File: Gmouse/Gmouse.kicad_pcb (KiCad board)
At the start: 2 copper layers, 121 x 100 mm, 1 part, among them U1 Teensy4.0

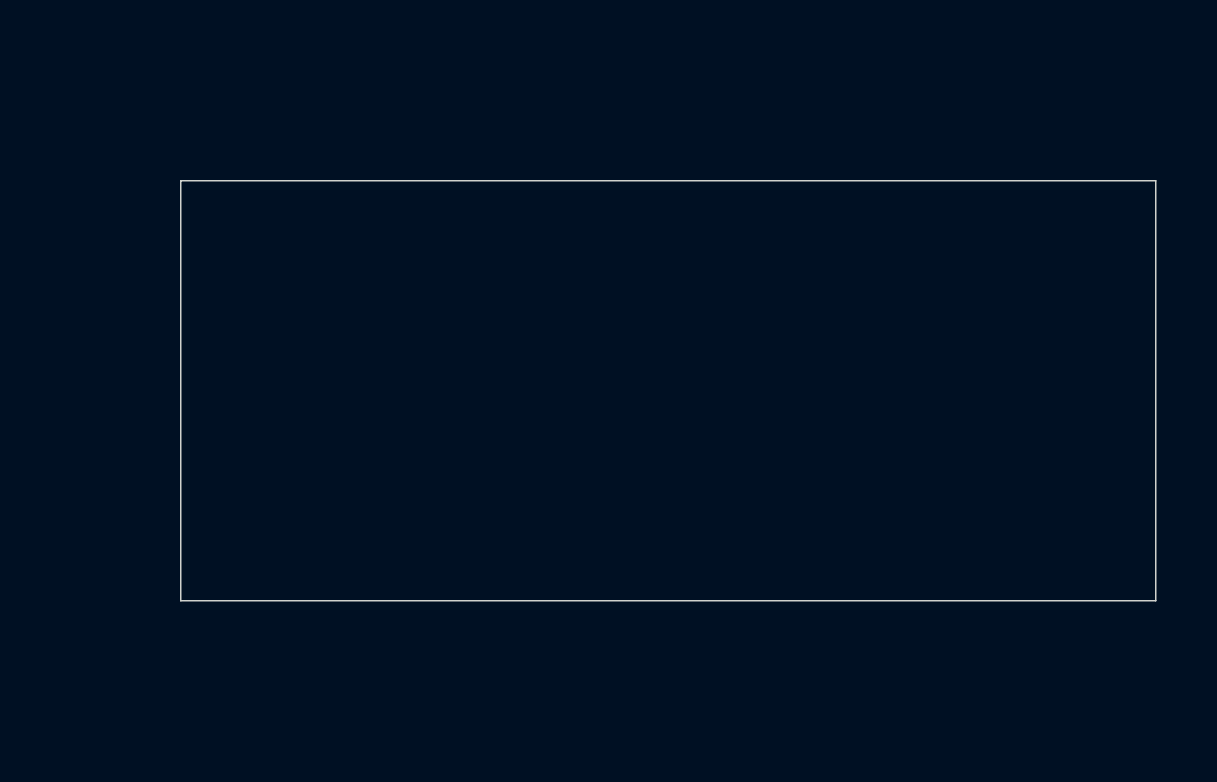
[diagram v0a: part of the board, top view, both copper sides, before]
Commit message: Adds basic motor circuitry and connectors, includes LED Display
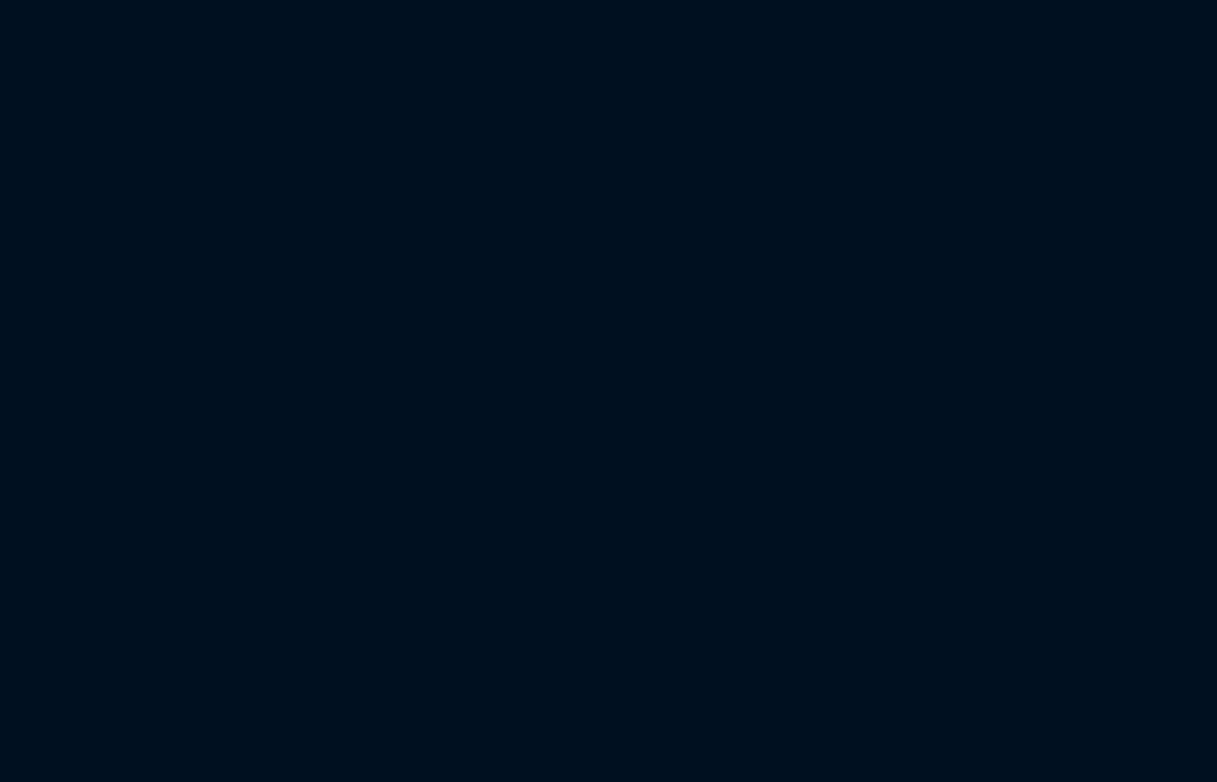
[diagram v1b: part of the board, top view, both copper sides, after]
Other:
- board size 121 x 100 mm -> 80 x 100 mm
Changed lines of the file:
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@@
 (kicad_pcb
-	(version 20240108)
+	(version 20241229)
 	(generator "pcbnew")
-	(generator_version "8.0")
+	(generator_version "9.0")
 	(general
 		(thickness 1.6)
@@
 	(layers
 		(0 "F.Cu" signal)
-		(31 "B.Cu" signal)
-		(32 "B.Adhes" user "B.Adhesive")
-		(33 "F.Adhes" user "F.Adhesive")
-		(34 "B.Paste" user)
-		(35 "F.Paste" user)
-		(36 "B.SilkS" user "B.Silkscreen")
-		(37 "F.SilkS" user "F.Silkscreen")
-		(38 "B.Mask" user)
-		(39 "F.Mask" user)
-		(40 "Dwgs.User" user "User.Drawings")
-		(41 "Cmts.User" user "User.Comments")
-		(42 "Eco1.User" user "User.Eco1")
-		(43 "Eco2.User" user "User.Eco2")
-		(44 "Edge.Cuts" user)
-		(45 "Margin" user)
-		(46 "B.CrtYd" user "B.Courtyard")
-		(47 "F.CrtYd" user "F.Courtyard")
-		(48 "B.Fab" user)
-		(49 "F.Fab" user)
-		(50 "User.1" user)
-		(51 "User.2" user)
-		(52 "User.3" user)
-		(53 "User.4" user)
-		(54 "User.5" user)
-		(55 "User.6" user)
-		(56 "User.7" user)
-		(57 "User.8" user)
-		(58 "User.9" user)
+		(2 "B.Cu" signal)
+		(9 "F.Adhes" user "F.Adhesive")
+		(11 "B.Adhes" user "B.Adhesive")
+		(13 "F.Paste" user)
+		(15 "B.Paste" user)
+		(5 "F.SilkS" user "F.Silkscreen")
+		(7 "B.SilkS" user "B.Silkscreen")
+		(1 "F.Mask" user)
+		(3 "B.Mask" user)
+		(17 "Dwgs.User" user "User.Drawings")
+		(19 "Cmts.User" user "User.Comments")
+		(21 "Eco1.User" user "User.Eco1")
+		(23 "Eco2.User" user "User.Eco2")
+		(25 "Edge.Cuts" user)
+		(27 "Margin" user)
+		(31 "F.CrtYd" user "F.Courtyard")
+		(29 "B.CrtYd" user "B.Courtyard")
+		(35 "F.Fab" user)
+		(33 "B.Fab" user)
+		(39 "User.1" user)
+		(41 "User.2" user)
+		(43 "User.3" user)
+		(45 "User.4" user)
+		(47 "User.5" user)
+		(49 "User.6" user)
+		(51 "User.7" user)
+		(53 "User.8" user)
+		(55 "User.9" user)
 	)
 	(setup
 		(pad_to_mask_clearance 0)
 		(allow_soldermask_bridges_in_footprints no)
+		(tenting front back)
 		(pcbplotparams
-			(layerselection 0x00010fc_ffffffff)
-			(plot_on_all_layers_selection 0x0000000_00000000)
+			(layerselection 0x00000000_00000000_55555555_5755f5ff)
+			(plot_on_all_layers_selection 0x00000000_00000000_00000000_00000000)
 			(disableapertmacros no)
 			(usegerberextensions no)
@@
 			(svgprecision 4)
 			(plotframeref no)
-			(viasonmask no)
 			(mode 1)
 			(useauxorigin no)
@@
 			(pdf_front_fp_property_popups yes)
 			(pdf_back_fp_property_popups yes)
+			(pdf_metadata yes)
+			(pdf_single_document no)
 			(dxfpolygonmode yes)
 			(dxfimperialunits yes)
@@
 			(psnegative no)
 			(psa4output no)
-			(plotreference yes)
-			(plotvalue yes)
-			(plotfptext yes)
+			(plot_black_and_white yes)
 			(plotinvisibletext no)
 			(sketchpadsonfab no)
+			(plotpadnumbers no)
+			(hidednponfab no)
+			(sketchdnponfab yes)
+			(crossoutdnponfab yes)
 			(subtractmaskfromsilk no)
 			(outputformat 1)
@@
 		(at 80 60 180)
 		(property "Reference" "U1"
-			(at 0 -10.16 360)
+			(at 0 -10.16 0)
 			(layer "F.SilkS")
 			(effects
@@
 		)
 		(property "Value" "Teensy4.0"
-			(at 0 10.16 360)
+			(at 0 10.16 0)
 			(layer "F.Fab")
 			(effects
@@
 			)
 		)
-		(property "Footprint" "Teensy:Teensy40_SMT"
-			(at 0 0 360)
+		(property "Datasheet" ""
+			(at 0 0 0)
 			(layer "F.Fab")
 			(hide yes)
@@
 			)
 		)
-		(property "Datasheet" ""
-			(at 0 0 360)
+		(property "Description" ""
+			(at 0 0 0)
 			(layer "F.Fab")
 			(hide yes)
@@
 			)
 		)
-		(property "Description" ""
-			(at 0 0 360)
-			(layer "F.Fab")
-			(hide yes)
-			(effects
-				(font
-					(size 1.27 1.27)
-					(thickness 0.15)
-				)
-			)
-		)
 		(sheetname "Root")
 		(sheetfile "Gmouse.kicad_sch")
@@
 				(type solid)
 			)
-			(fill solid)
+			(fill yes)
 			(layer "Eco1.User")
 		)
@@
 				(type solid)
 			)
-			(fill solid)
+			(fill yes)
 			(layer "Eco1.User")
 		)
@@
 				(type solid)
 			)
-			(fill solid)
+			(fill yes)
 			(layer "Eco1.User")
 		)
@@
 				(type solid)
 			)
-			(fill solid)
+			(fill yes)
 			(layer "Eco1.User")
 		)
@@
 				(type solid)
 			)
-			(fill solid)
+			(fill yes)
 			(layer "Eco1.User")
 		)
@@
 				(type solid)
 			)
-			(fill solid)
+			(fill yes)
 			(layer "Eco1.User")
 		)
@@
 				(type solid)
 			)
-			(fill solid)
+			(fill yes)
 			(layer "Eco1.User")
 		)
@@
 				(type solid)
 			)
-			(fill solid)
+			(fill yes)
 			(layer "Eco1.User")
 		)
@@
 				(type solid)
 			)
-			(fill solid)
+			(fill yes)
 			(layer "Eco1.User")
 		)
@@
 				(type solid)
 			)
-			(fill solid)
+			(fill yes)
 			(layer "Eco1.User")
 		)
@@
 				(type solid)
 			)
-			(fill solid)
+			(fill yes)
 			(layer "Eco1.User")
 		)
@@
 				(type solid)
 			)
-			(fill solid)
+			(fill yes)
 			(layer "Eco1.User")
 		)
@@
 				(type solid)
 			)
-			(fill solid)
+			(fill yes)
 			(layer "Eco1.User")
 		)
@@
 				(type solid)
 			)
-			(fill solid)
+			(fill yes)
 			(layer "Eco1.User")
 		)
@@
 				(type solid)
 			)
-			(fill solid)
+			(fill yes)
 			(layer "Eco1.User")
 		)
@@
 				(type solid)
 			)
-			(fill solid)
+			(fill yes)
 			(layer "Eco1.User")
 		)
@@
 				(type solid)
 			)
-			(fill solid)
+			(fill yes)
 			(layer "Eco1.User")
 		)
@@
 				(type solid)
 			)
-			(fill solid)
+			(fill yes)
 			(layer "Eco1.User")
 		)
@@
 				(type solid)
 			)
-			(fill solid)
+			(fill yes)
 			(layer "Eco1.User")
 		)
@@
 				(type solid)
 			)
-			(fill solid)
+			(fill yes)
 			(layer "Eco1.User")
 		)
@@
 			(pintype "bidirectional")
 		)
+		(embedded_fonts no)
 		(model "${KICAD_USER_DIR}/teensy.pretty/Teensy_4.0_Assembly.STEP"
 			(offset
@@
 			(type default)
 		)
-		(layer "Edge.Cuts")
-	)
-	(gr_rect
-		(start 128.5 62)
-		(end 161 76)
-		(stroke
-			(width 0.05)
-			(type default)
-		)
-		(fill none)
 		(layer "Edge.Cuts")
 	)
@@
 		(layer "Edge.Cuts")
 	)
+	(embedded_fonts no)
 )

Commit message: Pushing for desktop
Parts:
- moved U1 14.1 mm to (94.0, 58.0)
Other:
- outline, holes or cut-outs redrawn
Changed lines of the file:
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@@
 	(footprint "Teensy:Teensy40_SMT"
 		(layer "F.Cu")
-		(at 80 60 180)
+		(at 94 58 180)
 		(property "Reference" "U1"
 			(at 0 -10.16 0)
@@
 		(layer "Edge.Cuts")
 	)
-	(gr_arc
-		(start 40 70)
-		(mid 80 30)
-		(end 120 70)
+	(gr_line
+		(start 80 130)
+		(end 80 30)
+		(stroke
+			(width 0.05)
+			(type default)
+		)
+		(layer "Edge.Cuts")
+	)
+	(gr_curve
+		(pts
+			(xy 80 30) (xy 120 30) (xy 120 30) (xy 120 50)
+		)
 		(stroke
 			(width 0.05)
@@
 			(type default)
 		)
+		(locked yes)
+		(layer "Edge.Cuts")
+	)
+	(gr_curve
+		(pts
+			(xy 80 30) (xy 40 30) (xy 40 30) (xy 40 50)
+		)
+		(stroke
+			(width 0.05)
+			(type default)
+		)
 		(layer "Edge.Cuts")
 	)
@@
 	)
 	(gr_line
+		(start 40 50)
+		(end 40 70)
+		(stroke
+			(width 0.05)
+			(type default)
+		)
+		(layer "Edge.Cuts")
+	)
+	(gr_line
 		(start 106 70)
 		(end 120 70)
@@
 		(stroke
 			(width 0.05)
+			(type default)
+		)
+		(layer "Edge.Cuts")
+	)
+	(gr_line
+		(start 120 50)
+		(end 120 70)
+		(stroke
+			(width 0.05)

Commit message: Work Done Over Break
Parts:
- added BT1: 3.7V, Connector_JST:JST_PH_B2B-PH-K_1x02_P2.00mm_Vertical, F.Cu at (201.7, 83.1)
- added BT2: 3.7V, Connector_JST:JST_PH_B2B-PH-K_1x02_P2.00mm_Vertical, F.Cu at (201.7, 89.6)
- added C11: 4.7uF, Capacitor_SMD:C_1206_3216Metric_Pad1.33x1.80mm_HandSolder, F.Cu at (179.1, 82.0)
- added C12: 0.1uF, Capacitor_SMD:C_1206_3216Metric_Pad1.33x1.80mm_HandSolder, F.Cu at (179.1, 85.4)
- added C13: 4.7uF, Capacitor_SMD:C_1206_3216Metric_Pad1.33x1.80mm_HandSolder, F.Cu at (179.1, 88.7)
- added C14: 0.1uF, Capacitor_SMD:C_1206_3216Metric_Pad1.33x1.80mm_HandSolder, F.Cu at (179.1, 92.1)
- added C15: 4.7uF, Capacitor_SMD:C_1206_3216Metric_Pad1.33x1.80mm_HandSolder, F.Cu at (179.1, 95.4)
- added C16: 0.1uF, Capacitor_SMD:C_1206_3216Metric_Pad1.33x1.80mm_HandSolder, F.Cu at (179.1, 98.8)
- added C17: 4.7uF, Capacitor_SMD:C_1206_3216Metric_Pad1.33x1.80mm_HandSolder, F.Cu at (185.1, 82.0)
- added C18: 0.1uF, Capacitor_SMD:C_1206_3216Metric_Pad1.33x1.80mm_HandSolder, F.Cu at (185.1, 85.4)
- added C19: 4.7uF, Capacitor_SMD:C_1206_3216Metric_Pad1.33x1.80mm_HandSolder, F.Cu at (185.1, 88.7)
- added C2: 0.1 uF, Capacitor_SMD:C_1206_3216Metric_Pad1.33x1.80mm_HandSolder, F.Cu at (173.1, 82.0)
- added C20: 0.1uF, Capacitor_SMD:C_1206_3216Metric_Pad1.33x1.80mm_HandSolder, F.Cu at (185.1, 92.1)
- added C4: 0.1 uF, Capacitor_SMD:C_1206_3216Metric_Pad1.33x1.80mm_HandSolder, F.Cu at (173.1, 85.4)
- added C5: 4.7uF, Capacitor_SMD:C_1206_3216Metric_Pad1.33x1.80mm_HandSolder, F.Cu at (173.1, 88.7)
- added C6: 0.1uF, Capacitor_SMD:C_1206_3216Metric_Pad1.33x1.80mm_HandSolder, F.Cu at (173.1, 92.1)
- added C7: 0.1 uF, Capacitor_SMD:C_1206_3216Metric_Pad1.33x1.80mm_HandSolder, F.Cu at (173.1, 95.4)
- added C9: 0.1 uF, Capacitor_SMD:C_1206_3216Metric_Pad1.33x1.80mm_HandSolder, F.Cu at (173.1, 98.8)
- added D1: IR, LED_THT:LED_D5.0mm_Horizontal_O1.27mm_Z9.0mm, F.Cu at (142.6, 40.1)
- added D2: IR, LED_THT:LED_D5.0mm_Horizontal_O1.27mm_Z9.0mm, F.Cu at (150.1, 40.1)
- added D3: IR, LED_THT:LED_D5.0mm_Horizontal_O1.27mm_Z9.0mm, F.Cu at (157.6, 40.1)
- added D4: IR, LED_THT:LED_D5.0mm_Horizontal_O1.27mm_Z9.0mm, F.Cu at (165.1, 40.1)
- added D5: IR, LED_THT:LED_D5.0mm_Horizontal_O1.27mm_Z9.0mm, F.Cu at (142.6, 52.6)
- added D6: IR, LED_THT:LED_D5.0mm_Horizontal_O1.27mm_Z9.0mm, F.Cu at (150.1, 52.6)
- added J1: Motor_RF, Connector_JST:JST_SH_BM05B-SRSS-TB_1x05-1MP_P1.00mm_Vertical, F.Cu at (145.1, 78.8)
- added J2: Motor_RR, Connector_JST:JST_SH_BM05B-SRSS-TB_1x05-1MP_P1.00mm_Vertical, F.Cu at (145.1, 85.1)
- added J3: Motor_LF, Connector_JST:JST_SH_BM05B-SRSS-TB_1x05-1MP_P1.00mm_Vertical, F.Cu at (145.1, 91.3)
- added J4: Motor_LR, Connector_JST:JST_SH_BM05B-SRSS-TB_1x05-1MP_P1.00mm_Vertical, F.Cu at (145.1, 97.6)
- added J5: Conn_01x08_Pin, Connector_PinSocket_2.54mm:PinSocket_1x08_P2.54mm_Vertical, F.Cu at (85.2, 57.0)
- added LS1: SMT-0440-T-R, SMT_0440:XDCR_SMT-0440-T-R, F.Cu at (198.5, 68.4)
- added Q10: SFH300, LED_THT:LED_D5.0mm_Horizontal_O1.27mm_Z3.0mm_IRGrey, F.Cu at (157.6, 65.0)
- added Q12: SFH300, LED_THT:LED_D5.0mm_Horizontal_O1.27mm_Z3.0mm_IRGrey, F.Cu at (165.1, 65.0)
- added Q14: BC847, Package_TO_SOT_SMD:SOT-23, F.Cu at (202.5, 73.6)
- added Q2: SFH300, LED_THT:LED_D5.0mm_Horizontal_O1.27mm_Z3.0mm_IRGrey, F.Cu at (157.6, 52.6)
- added Q4: SFH300, LED_THT:LED_D5.0mm_Horizontal_O1.27mm_Z3.0mm_IRGrey, F.Cu at (165.1, 52.6)
- added Q6: SFH300, LED_THT:LED_D5.0mm_Horizontal_O1.27mm_Z3.0mm_IRGrey, F.Cu at (142.6, 65.0)
- added Q8: SFH300, LED_THT:LED_D5.0mm_Horizontal_O1.27mm_Z3.0mm_IRGrey, F.Cu at (150.1, 65.0)
- added R1: 47K, Resistor_SMD:R_1206_3216Metric_Pad1.30x1.75mm_HandSolder, F.Cu at (173.1, 59.0)
- added R10: 47K, Resistor_SMD:R_1206_3216Metric_Pad1.30x1.75mm_HandSolder, F.Cu at (179.0, 65.5)
- added R11: 51, Resistor_SMD:R_1206_3216Metric_Pad1.30x1.75mm_HandSolder, F.Cu at (179.0, 68.8)
- added R12: 1.8K, Resistor_SMD:R_1206_3216Metric_Pad1.30x1.75mm_HandSolder, F.Cu at (179.0, 72.1)
- added R13: 100, Resistor_SMD:R_1206_3216Metric_Pad1.30x1.75mm_HandSolder, F.Cu at (179.0, 75.4)
- added R14: 47K, Resistor_SMD:R_1206_3216Metric_Pad1.30x1.75mm_HandSolder, F.Cu at (179.0, 78.7)
- added R15: 51, Resistor_SMD:R_1206_3216Metric_Pad1.30x1.75mm_HandSolder, F.Cu at (185.0, 59.0)
- added R16: 1.8K, Resistor_SMD:R_1206_3216Metric_Pad1.30x1.75mm_HandSolder, F.Cu at (185.0, 62.3)
- added R17: 100, Resistor_SMD:R_1206_3216Metric_Pad1.30x1.75mm_HandSolder, F.Cu at (185.0, 65.5)
- added R18: 47K, Resistor_SMD:R_1206_3216Metric_Pad1.30x1.75mm_HandSolder, F.Cu at (185.0, 68.8)
- added R19: 51, Resistor_SMD:R_1206_3216Metric_Pad1.30x1.75mm_HandSolder, F.Cu at (185.0, 72.1)
- added R2: 100, Resistor_SMD:R_1206_3216Metric_Pad1.30x1.75mm_HandSolder, F.Cu at (173.1, 62.3)
- added R20: 1.8K, Resistor_SMD:R_1206_3216Metric_Pad1.30x1.75mm_HandSolder, F.Cu at (185.0, 75.4)
- added R21: 100, Resistor_SMD:R_1206_3216Metric_Pad1.30x1.75mm_HandSolder, F.Cu at (185.0, 78.7)
- added R22: 47K, Resistor_SMD:R_1206_3216Metric_Pad1.30x1.75mm_HandSolder, F.Cu at (190.9, 59.0)
- added R23: 51, Resistor_SMD:R_1206_3216Metric_Pad1.30x1.75mm_HandSolder, F.Cu at (190.9, 62.3)
- added R24: 1.8K, Resistor_SMD:R_1206_3216Metric_Pad1.30x1.75mm_HandSolder, F.Cu at (190.9, 65.5)
- added R25: 180, Resistor_SMD:R_1206_3216Metric_Pad1.30x1.75mm_HandSolder, F.Cu at (190.9, 68.8)
- added R3: 51, Resistor_SMD:R_1206_3216Metric_Pad1.30x1.75mm_HandSolder, F.Cu at (173.1, 65.5)
- added R4: 1.8K, Resistor_SMD:R_1206_3216Metric_Pad1.30x1.75mm_HandSolder, F.Cu at (173.1, 68.8)
- added R5: 100, Resistor_SMD:R_1206_3216Metric_Pad1.30x1.75mm_HandSolder, F.Cu at (173.1, 72.1)
- added R6: 47K, Resistor_SMD:R_1206_3216Metric_Pad1.30x1.75mm_HandSolder, F.Cu at (173.1, 75.4)
- added R7: 51, Resistor_SMD:R_1206_3216Metric_Pad1.30x1.75mm_HandSolder, F.Cu at (173.1, 78.7)
- added R8: 1.8K, Resistor_SMD:R_1206_3216Metric_Pad1.30x1.75mm_HandSolder, F.Cu at (179.0, 59.0)
- added R9: 100, Resistor_SMD:R_1206_3216Metric_Pad1.30x1.75mm_HandSolder, F.Cu at (179.0, 62.3)
- added REF**: JST_PH_B2B-PH-K_1x02_P2.00mm_Vertical, Connector_JST:JST_PH_B2B-PH-K_1x02_P2.00mm_Vertical, F.Cu at (66.0, 68.0)
- added REF**: JST_SH_BM06B-SRSS-TB_1x06-1MP_P1.00mm_Vertical, Connector_JST:JST_SH_BM06B-SRSS-TB_1x06-1MP_P1.00mm_Vertical, F.Cu at (91.0, 134.0)
- added REF**: JST_SH_BM06B-SRSS-TB_1x06-1MP_P1.00mm_Vertical, Connector_JST:JST_SH_BM06B-SRSS-TB_1x06-1MP_P1.00mm_Vertical, F.Cu at (73.0, 134.0)
- added REF**: DIP12_HCMS-290X-A_BRA, HCMS_2903:DIP12_HCMS-290X-A_BRA, F.Cu at (98.0, 137.0)
- added REF**: JST_SH_BM06B-SRSS-TB_1x06-1MP_P1.00mm_Vertical, Connector_JST:JST_SH_BM06B-SRSS-TB_1x06-1MP_P1.00mm_Vertical, F.Cu at (79.0, 134.0)
- added REF**: Teensy 4.0, Teensy:Teensy40_SMT, F.Cu at (115.0, 68.0)
- added REF**: SW_TL3365AF180QG, Buttons:SW_TL3365AF180QG, F.Cu at (116.0, 129.0)
- added REF**: XDCR_SMT-0440-T-R, SMT_0440:XDCR_SMT-0440-T-R, F.Cu at (61.0, 76.0)
- added REF**: SW_TL3365AF180QG, Buttons:SW_TL3365AF180QG, F.Cu at (116.0, 136.0)
- added REF**: JST_PH_B2B-PH-K_1x02_P2.00mm_Vertical, Connector_JST:JST_PH_B2B-PH-K_1x02_P2.00mm_Vertical, F.Cu at (76.0, 68.0)
- added REF**: JST_SH_BM06B-SRSS-TB_1x06-1MP_P1.00mm_Vertical, Connector_JST:JST_SH_BM06B-SRSS-TB_1x06-1MP_P1.00mm_Vertical, F.Cu at (85.0, 134.0)
- added U2: TB6612FNG, Package_SO:SSOP-24_5.3x8.2mm_P0.65mm, F.Cu at (193.4, 85.4)
- added U3: L78L05_SOT89, Package_TO_SOT_SMD:SOT-89-3, F.Cu at (197.3, 74.3)
- added U4: HCMS-2903, HCMS_2903:DIP12_HCMS-290X-A_BRA, F.Cu at (152.1, 79.1)
- added U5: TB6612FNG, Package_SO:SSOP-24_5.3x8.2mm_P0.65mm, F.Cu at (193.4, 95.4)
- added U7: LD1117S33TR_SOT223, Package_TO_SOT_SMD:SOT-223-3_TabPin2, F.Cu at (198.8, 61.5)
- moved U1 96.3 mm to (189.7, 47.9), turned to 0 degrees
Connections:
- U1 pad 1: unconnected-(U1-GND-Pad1) -> GND
- U1 pad 17: unconnected-(U1-GND-Pad17) -> GND
- U1 pad 32: unconnected-(U1-GND-Pad32) -> GND
- U1 pad 33: unconnected-(U1-VIN-Pad33) -> +5V
- U1 pad 4: unconnected-(U1-2_OUT2-Pad4) -> IR_Emmiter_Left_Half
- U1 pad 5: unconnected-(U1-3_LRCLK2-Pad5) -> IR_Emmiter_Right_Half
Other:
- outline, holes or cut-outs redrawn
